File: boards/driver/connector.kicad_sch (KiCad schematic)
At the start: 1 part, among them J5 DIN41612_03x32_C

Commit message: Driver: Added a 5V->3.3V LDO to replace the reversed cmod header, added jumpers for the 200R parallel returns, and renamed subcircuit ports to avoid unexpected ground connections.
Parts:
- renumbered J5 to J1
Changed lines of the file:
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@@
   (symbol (lib_id "lachesis:DIN41612_03x32_C") (at 92.71 80.01 0) (unit 1)
     (in_bom yes) (on_board yes)
-    (property "Reference" "J5" (id 0) (at 91.44 134.62 0)
+    (property "Reference" "J1" (id 0) (at 91.44 134.62 0)
       (effects (font (size 1.27 1.27)) (justify left))
     )
@@
   (symbol (lib_id "lachesis:DIN41612_03x32_C") (at 132.08 80.01 0) (unit 2)
     (in_bom yes) (on_board yes)
-    (property "Reference" "J5" (id 0) (at 130.81 134.62 0)
+    (property "Reference" "J1" (id 0) (at 130.81 134.62 0)
       (effects (font (size 1.27 1.27)) (justify left))
     )
@@
   (symbol (lib_id "lachesis:DIN41612_03x32_C") (at 173.99 80.01 0) (unit 3)
     (in_bom yes) (on_board yes)
-    (property "Reference" "J5" (id 0) (at 172.72 134.62 0)
+    (property "Reference" "J1" (id 0) (at 172.72 134.62 0)
       (effects (font (size 1.27 1.27)) (justify left))
     )
@@
   (symbol (lib_id "power:GND") (at 121.92 102.87 0) (unit 1)
     (in_bom yes) (on_board yes)
-    (property "Reference" "#PWR0158" (id 0) (at 121.92 109.22 0)
+    (property "Reference" "#PWR0121" (id 0) (at 121.92 109.22 0)
       (effects (font (size 1.27 1.27)) hide)
     )

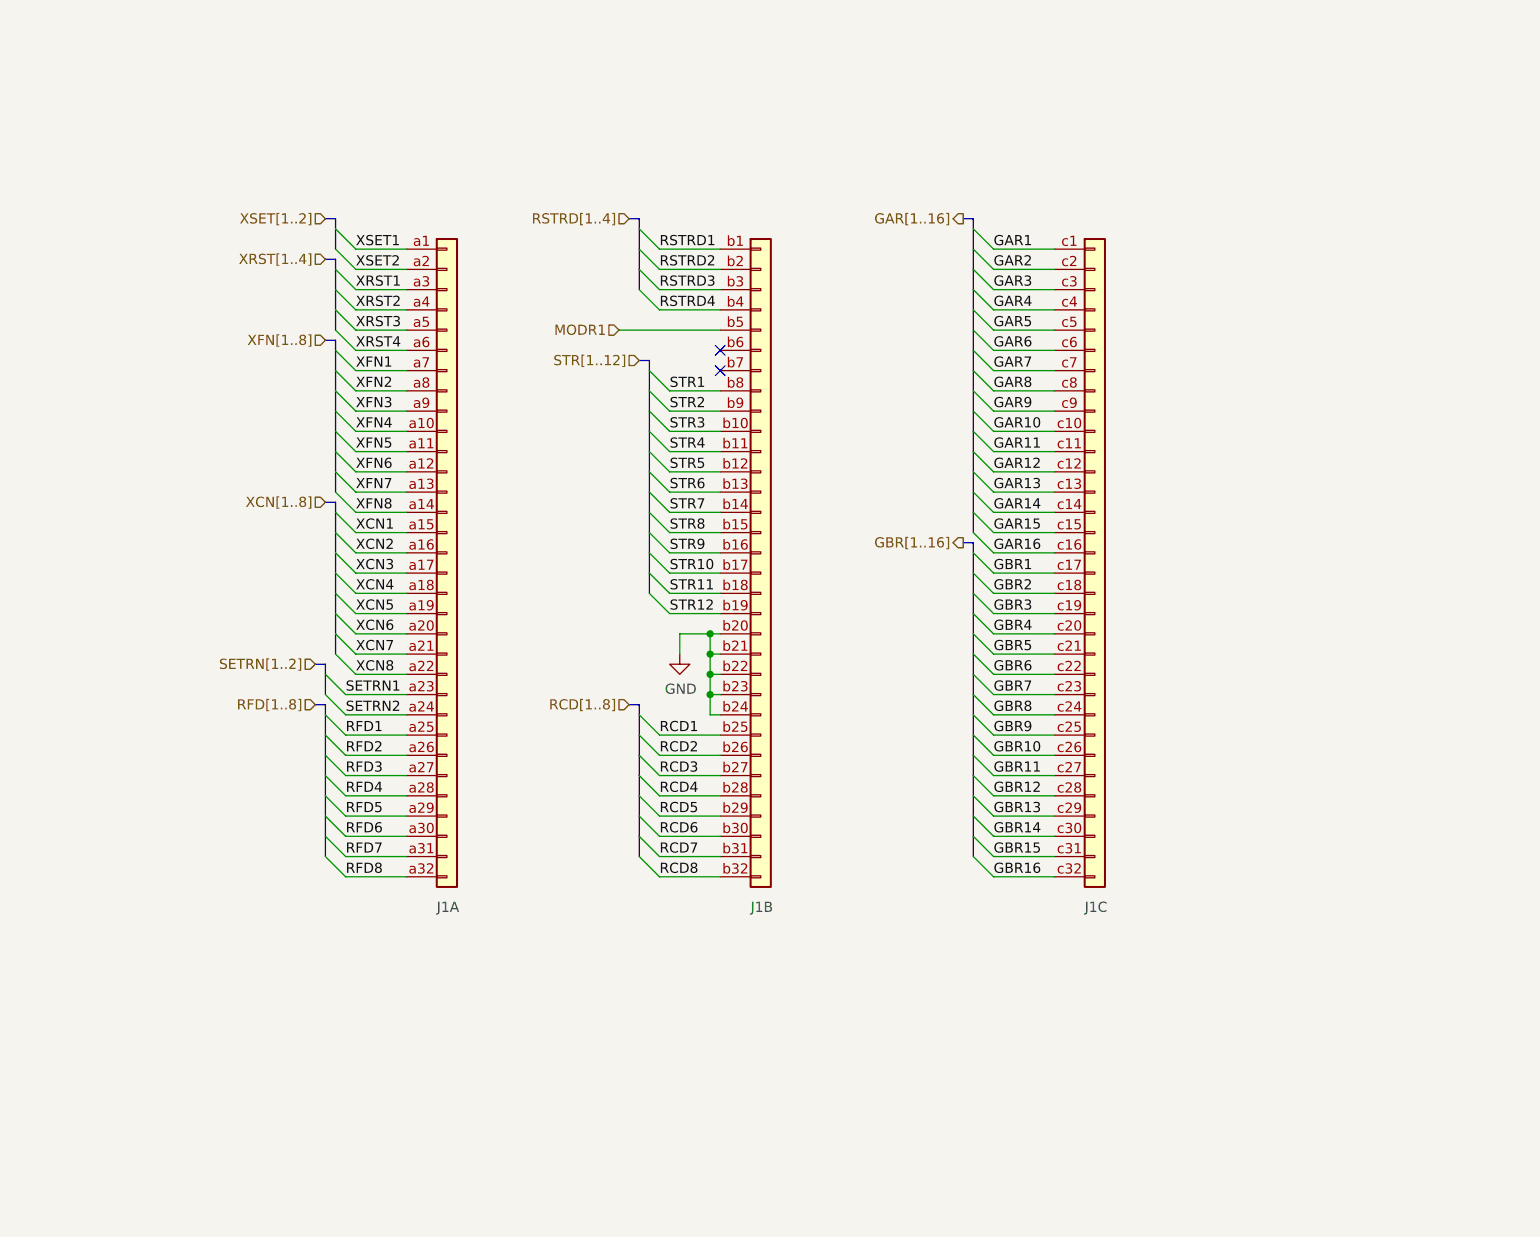
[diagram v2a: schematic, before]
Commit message: Driver: laid out most of the subcircuits
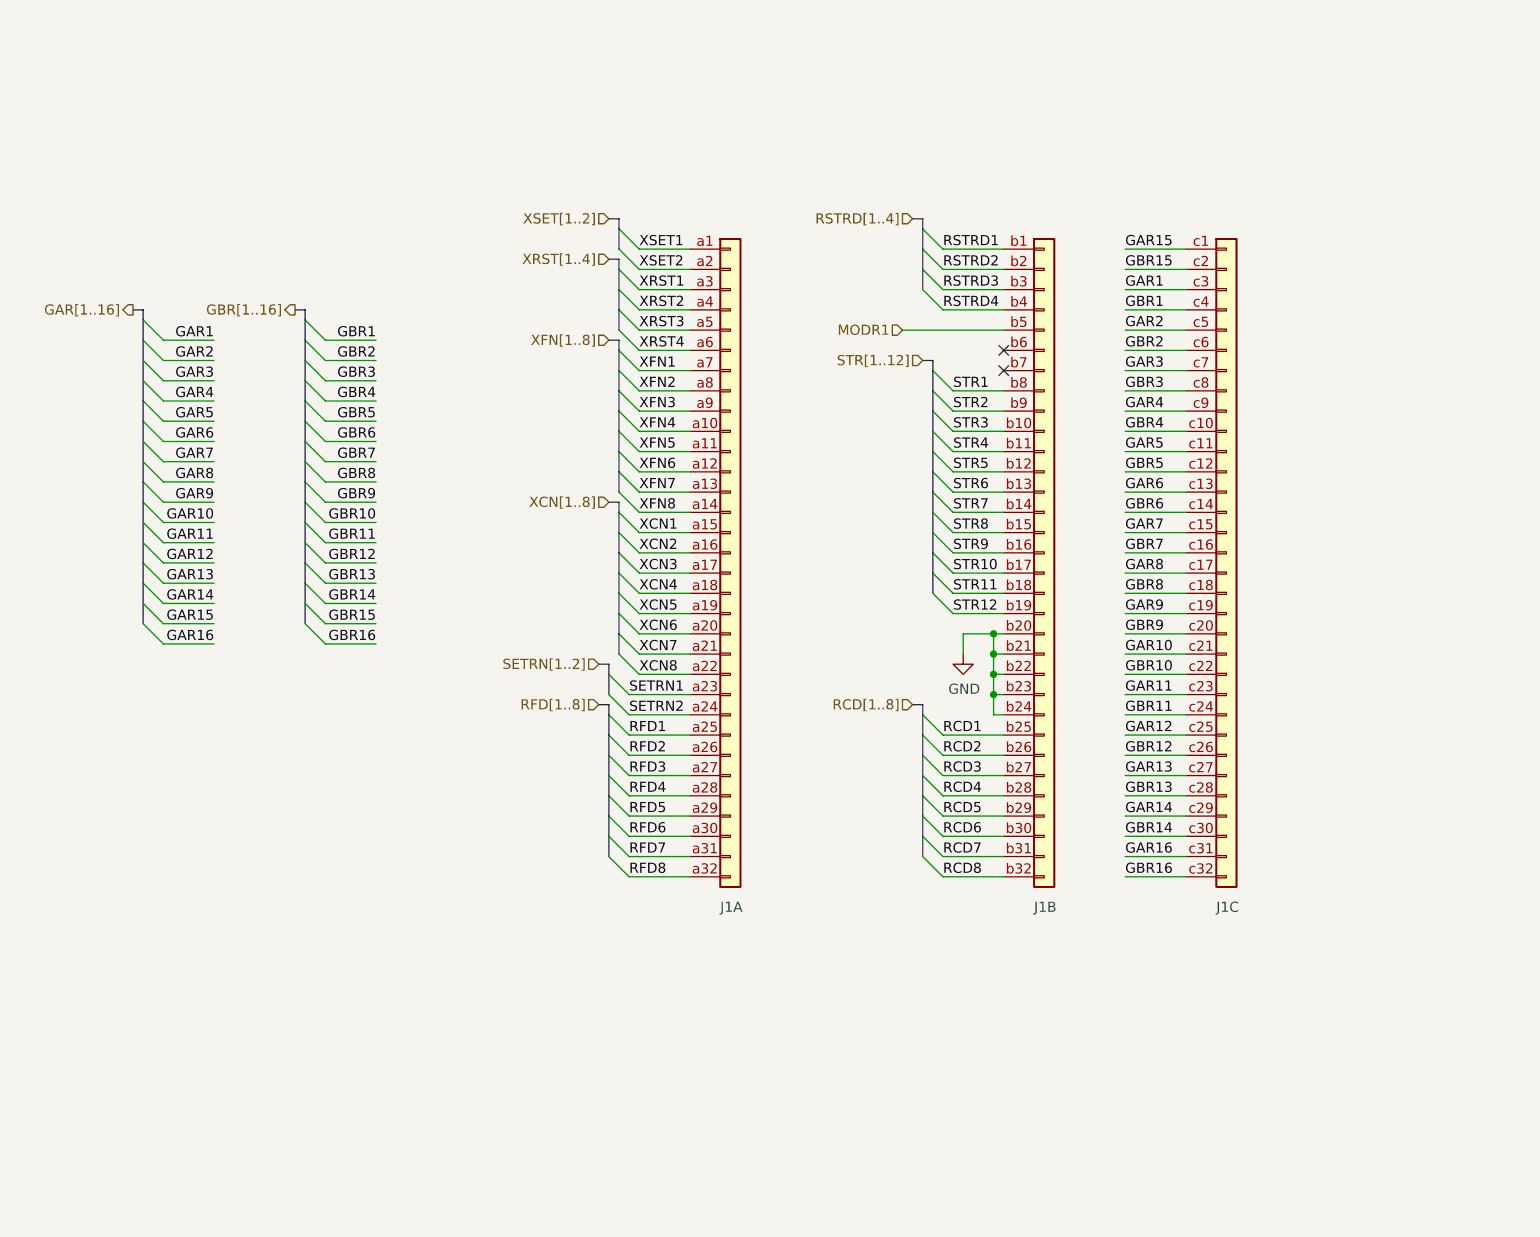
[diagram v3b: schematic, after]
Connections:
- net GAR1: now also J1.c3; no longer J1.c1
- net GAR10: now also J1.c21; no longer J1.c10
- net GAR11: now also J1.c23; no longer J1.c11
- net GAR12: now also J1.c25; no longer J1.c12
- net GAR13: now also J1.c27; no longer J1.c13
- net GAR14: now also J1.c29; no longer J1.c14
- net GAR15: now also J1.c1; no longer J1.c15
- net GAR16: now also J1.c31; no longer J1.c16
- net GAR2: now also J1.c5; no longer J1.c2
- net GAR3: now also J1.c7; no longer J1.c3
- net GAR4: now also J1.c9; no longer J1.c4
- net GAR5: now also J1.c11; no longer J1.c5
- net GAR6: now also J1.c13; no longer J1.c6
- net GAR7: now also J1.c15; no longer J1.c7
- net GAR8: now also J1.c17; no longer J1.c8
- net GAR9: now also J1.c19; no longer J1.c9
- net GBR1: now also J1.c4; no longer J1.c17
- net GBR10: now also J1.c22; no longer J1.c26
- net GBR11: now also J1.c24; no longer J1.c27
- net GBR12: now also J1.c26; no longer J1.c28
- net GBR13: now also J1.c28; no longer J1.c29
- net GBR15: now also J1.c2; no longer J1.c31
- net GBR2: now also J1.c6; no longer J1.c18
- net GBR3: now also J1.c8; no longer J1.c19
- net GBR4: now also J1.c10; no longer J1.c20
- net GBR5: now also J1.c12; no longer J1.c21
- net GBR6: now also J1.c14; no longer J1.c22
- net GBR7: now also J1.c16; no longer J1.c23
- net GBR8: now also J1.c18; no longer J1.c24
- net GBR9: now also J1.c20; no longer J1.c25
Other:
- moved on the sheet: J1A, J1B, J1C

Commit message: Driver: incorporated completed backplane pinout and did a little bit more routing on the board
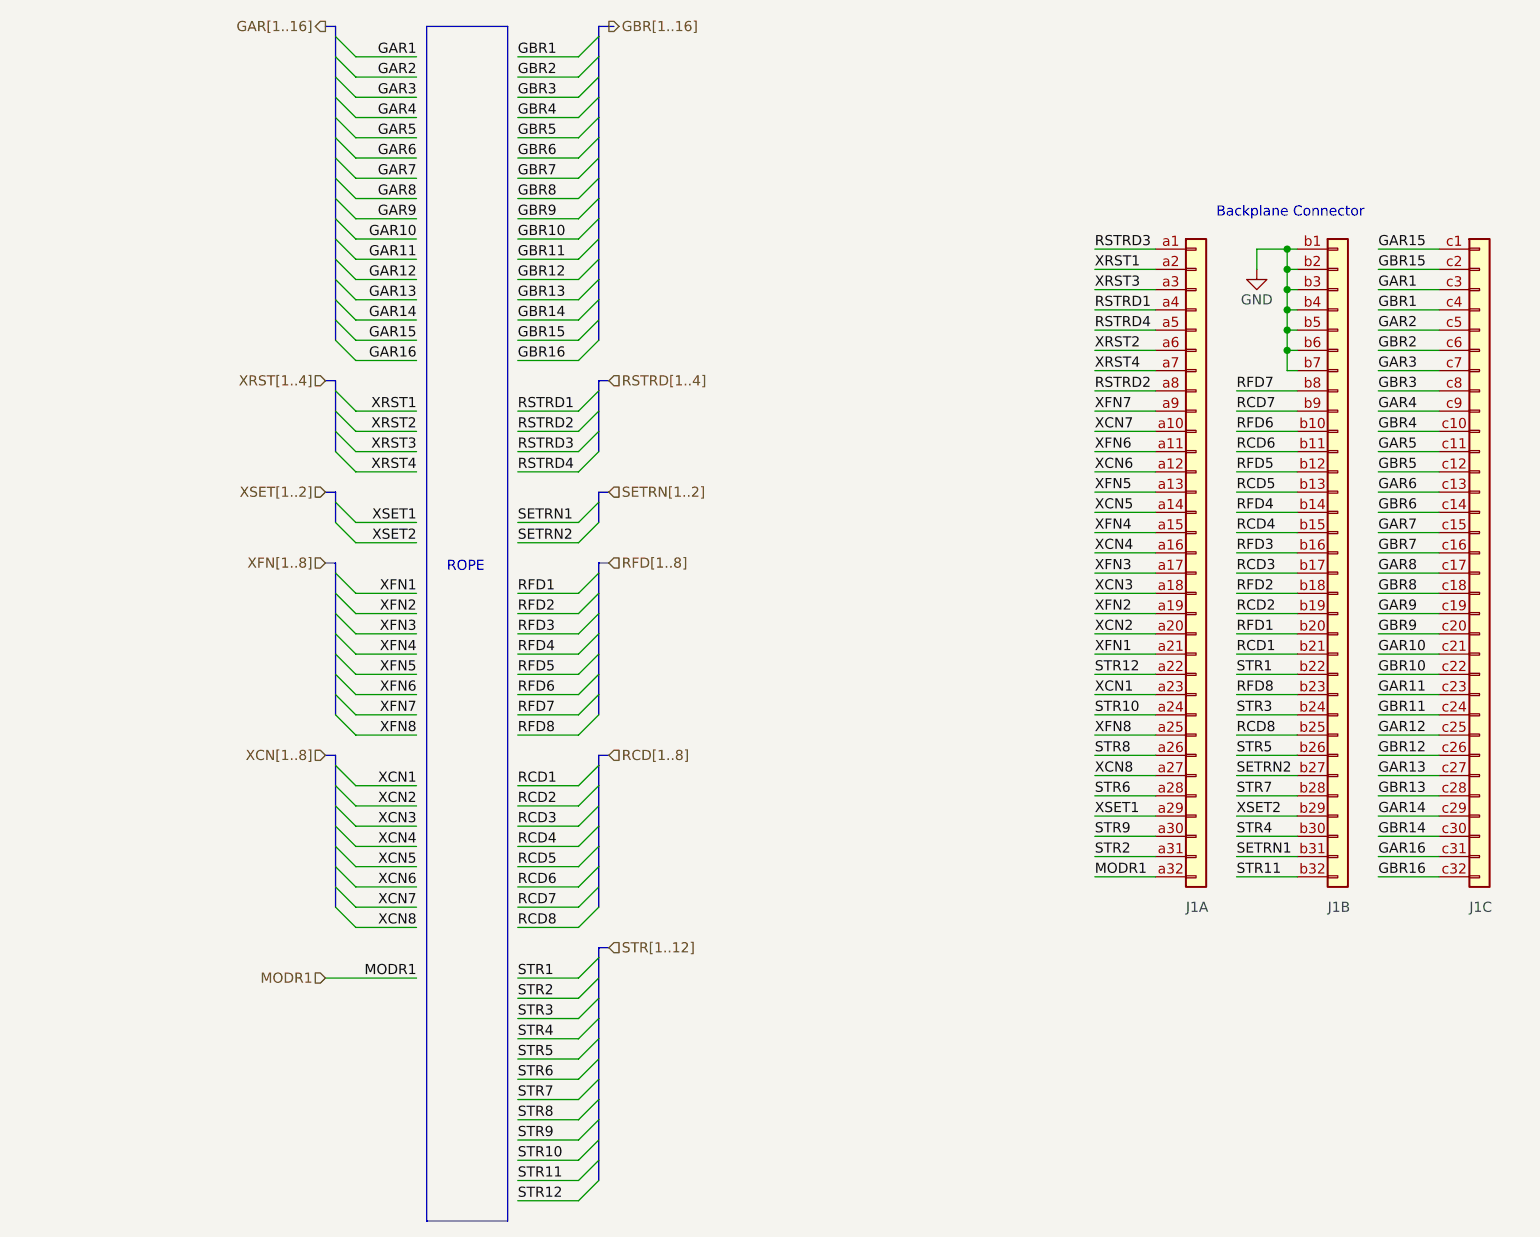
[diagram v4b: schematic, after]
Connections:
- net GND: now also J1.b1, J1.b2, J1.b3, J1.b4, J1.b5, J1.b6, J1.b7; no longer J1.b20, J1.b21, J1.b22, J1.b23, J1.b24
- net MODR1: now also J1.a32; no longer J1.b5
- net RCD1: now also J1.b21; no longer J1.b25
- net RCD2: now also J1.b19; no longer J1.b26
- net RCD3: now also J1.b17; no longer J1.b27
- net RCD4: now also J1.b15; no longer J1.b28
- net RCD5: now also J1.b13; no longer J1.b29
- net RCD6: now also J1.b11; no longer J1.b30
- net RCD7: now also J1.b9; no longer J1.b31
- net RCD8: now also J1.b25; no longer J1.b32
- net RFD1: now also J1.b20; no longer J1.a25
- net RFD2: now also J1.b18; no longer J1.a26
- net RFD3: now also J1.b16; no longer J1.a27
- net RFD4: now also J1.b14; no longer J1.a28
- net RFD5: now also J1.b12; no longer J1.a29
- net RFD6: now also J1.b10; no longer J1.a30
- net RFD7: now also J1.b8; no longer J1.a31
- net RFD8: now also J1.b23; no longer J1.a32
- net RSTRD1: now also J1.a4; no longer J1.b1
- net RSTRD2: now also J1.a8; no longer J1.b2
- net RSTRD3: now also J1.a1; no longer J1.b3
- net RSTRD4: now also J1.a5; no longer J1.b4
- net SETRN1: now also J1.b31; no longer J1.a23
- net SETRN2: now also J1.b27; no longer J1.a24
- net STR1: now also J1.b22; no longer J1.b8
- net STR10: now also J1.a24; no longer J1.b17
- net STR11: now also J1.b32; no longer J1.b18
- net STR12: now also J1.a22; no longer J1.b19
- net STR2: now also J1.a31; no longer J1.b9
- net STR3: now also J1.b24; no longer J1.b10
- net STR4: now also J1.b30; no longer J1.b11
- net STR5: now also J1.b26; no longer J1.b12
- net STR6: now also J1.a28; no longer J1.b13
- net STR7: now also J1.b28; no longer J1.b14
- net STR8: now also J1.a26; no longer J1.b15
- net STR9: now also J1.a30; no longer J1.b16
- net XCN1: now also J1.a23; no longer J1.a15
- net XCN2: now also J1.a20; no longer J1.a16
- net XCN3: now also J1.a18; no longer J1.a17
- net XCN4: now also J1.a16; no longer J1.a18
- net XCN5: now also J1.a14; no longer J1.a19
- net XCN6: now also J1.a12; no longer J1.a20
- net XCN7: now also J1.a10; no longer J1.a21
- net XCN8: now also J1.a27; no longer J1.a22
- net XFN1: now also J1.a21; no longer J1.a7
- net XFN2: now also J1.a19; no longer J1.a8
- net XFN3: now also J1.a17; no longer J1.a9
- net XFN4: now also J1.a15; no longer J1.a10
- net XFN5: now also J1.a13; no longer J1.a11
- net XFN6: now also J1.a11; no longer J1.a12
- net XFN7: now also J1.a9; no longer J1.a13
- net XFN8: now also J1.a25; no longer J1.a14
- net XRST1: now also J1.a2; no longer J1.a3
- net XRST2: now also J1.a6; no longer J1.a4
- net XRST3: now also J1.a3; no longer J1.a5
- net XRST4: now also J1.a7; no longer J1.a6
- net XSET1: now also J1.a29; no longer J1.a1
- net XSET2: now also J1.b29; no longer J1.a2
- no-connect marks 2 -> 0
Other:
- note added: "Backplane Connector"
- note added: "ROPE"
- moved on the sheet: J1A, J1B, J1C
